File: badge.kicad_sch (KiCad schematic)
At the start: 29 parts, among them J1 SAO V.1.69bis master, Q1 BSS138, SW1 power, SW2 SW_Push, SW3 update epaper, U1 Seeed XIAO ESP32-C3, U2 epaper2.13, U3 5V boost converter, U4 TXS0104EPWR

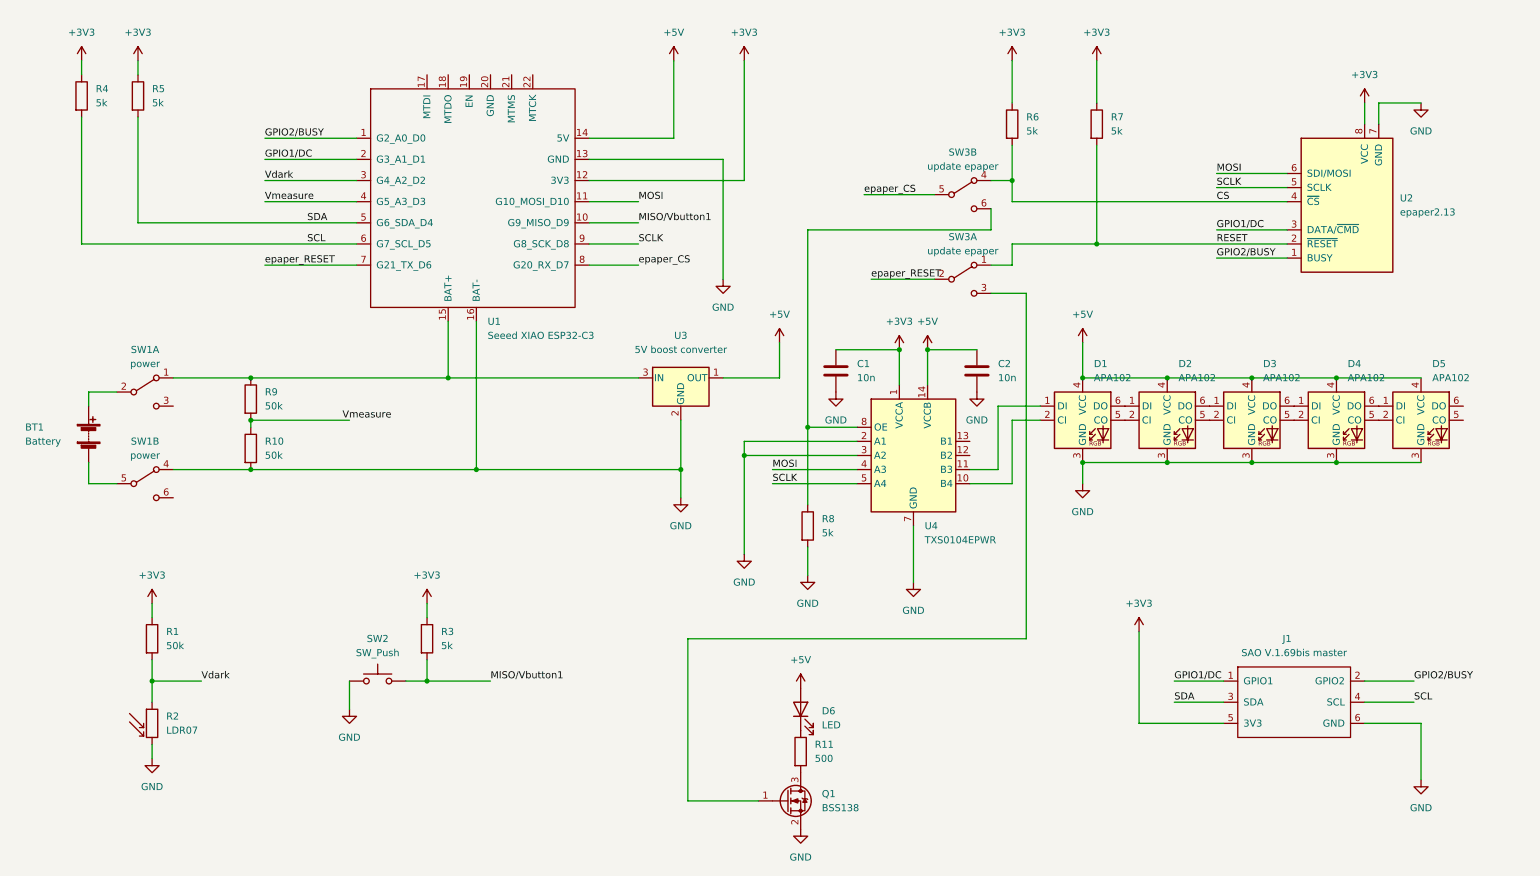
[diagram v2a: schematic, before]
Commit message: disable epaper mod by cutting power (also helps lifetime)
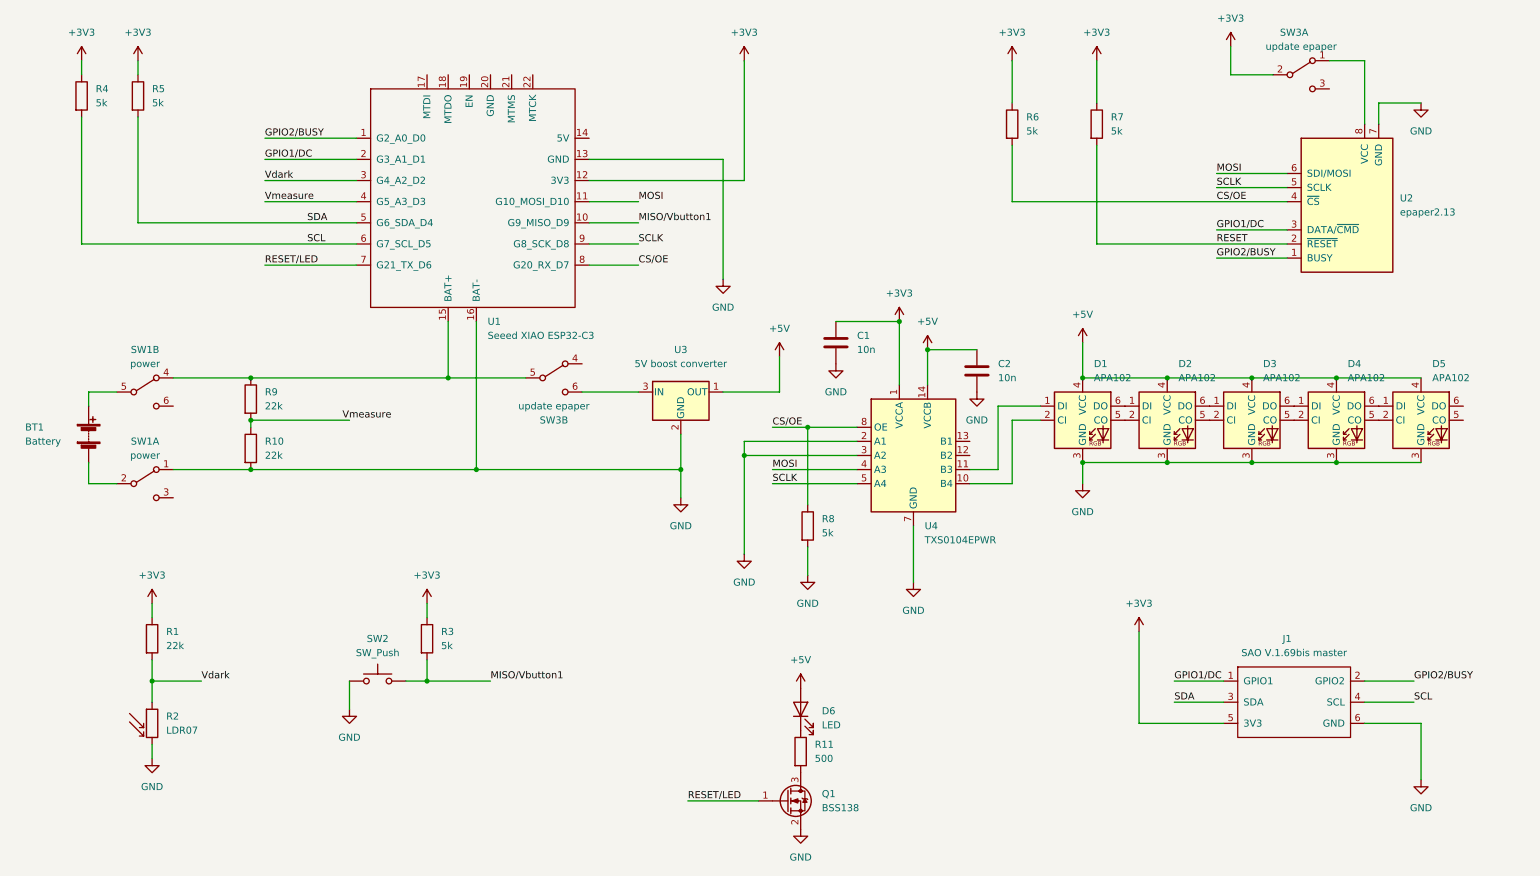
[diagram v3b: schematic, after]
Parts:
- R1, R10, R9: value 50k -> 22k
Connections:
- net +3V3: now also SW3.2 (B); no longer U2.8 (VCC)
- net +5V: no longer U1.14 (5V)
- net GND: now also SW1.1 (A); no longer SW1.4 (A)
- net RESET: no longer SW3.1 (A)
- net at R9.1, U1.15 (BAT+): now also SW1.4 (A), SW3.5 (B); no longer SW1.1 (A), U3.3 (IN)
- net at SW1.2 (B): now also BT1.2 (-); no longer BT1.1 (+)
- net CS/OE: now reaches R8.1, U4.8 (OE)
- net CS/OE: now also R6.2, U1.8 (G20_RX_D7), U2.4 (~{CS}); no longer SW3.6 (C)
- net at SW1.5 (B): now also BT1.1 (+); no longer BT1.2 (-)
- net at SW3.3 (C): no longer Q1.1 (G)
- removed net CS: R6.2, SW3.4 (A), U2.4 (~{CS})
- removed net epaper_CS: SW3.5 (B), U1.8 (G20_RX_D7)
- net epaper_RESET renamed RESET/LED
- net RESET/LED: now also Q1.1 (G); no longer SW3.2 (B)
- new net: SW3.1 (A), U2.8 (VCC)
- new net: SW3.6 (C), U3.3 (IN)
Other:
- moved on the sheet: C1, SW1A, SW1B, SW3A, SW3B, U3

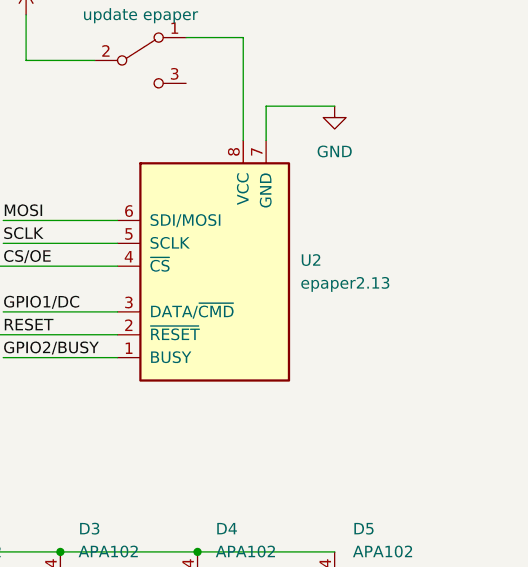
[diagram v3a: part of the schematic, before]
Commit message: use updated epaper footprint
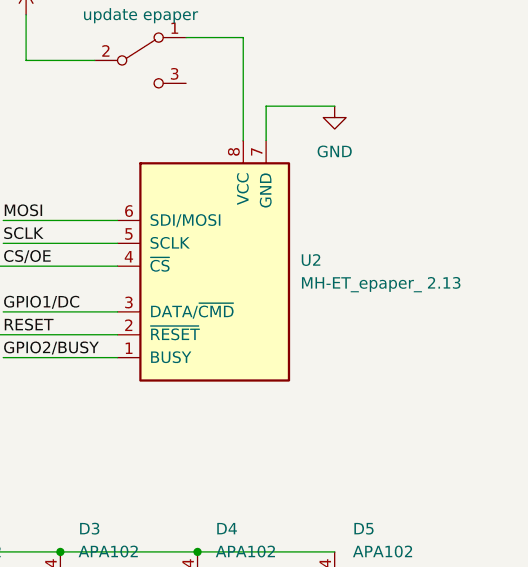
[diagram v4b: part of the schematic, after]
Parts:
- U2: value epaper2.13 -> MH-ET_epaper_ 2.13; footprint extra:epaper2.13 -> extra:MH-ET_epaper_ 2.13; symbol mlp:epaper2.13 -> extra:MH-ET_epaper_ 2.13
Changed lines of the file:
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@@
     (pin "6")
   )
-  (symbol (lib_id "mlp:epaper2.13") (at 254 52.07 0) (unit 1)
+  (symbol (lib_id "extra:MH-ET_epaper_ 2.13") (at 254 52.07 0) (unit 1)
     (in_bom yes) (on_board yes) (fields_autoplaced)
     (property "Reference" "U2" (id 0) (at 264.16 48.8949 0)
       (effects (font (size 1.27 1.27)) (justify left))
     )
-    (property "Value" "epaper2.13" (id 1) (at 264.16 51.4349 0)
-      (effects (font (size 1.27 1.27)) (justify left))
-    )
-    (property "Footprint" "extra:epaper2.13" (id 2) (at 254 66.04 0)
+    (property "Value" "MH-ET_epaper_ 2.13" (id 1) (at 264.16 51.4349 0)
+      (effects (font (size 1.27 1.27)) (justify left))
+    )
+    (property "Footprint" "extra:MH-ET_epaper_ 2.13" (id 2) (at 254 66.04 0)
       (effects (font (size 1.27 1.27)) hide)
     )
@@
     )
     (path "/20ddfe2b-2a25-4b87-9377-bd1690073b28"
-      (reference "U2") (unit 1) (value "epaper2.13") (footprint "extra:epaper2.13")
+      (reference "U2") (unit 1) (value "MH-ET_epaper_ 2.13") (footprint "extra:MH-ET_epaper_ 2.13")
     )
     (path "/45af8bb5-3b53-4556-9240-4d30d2024c6a"

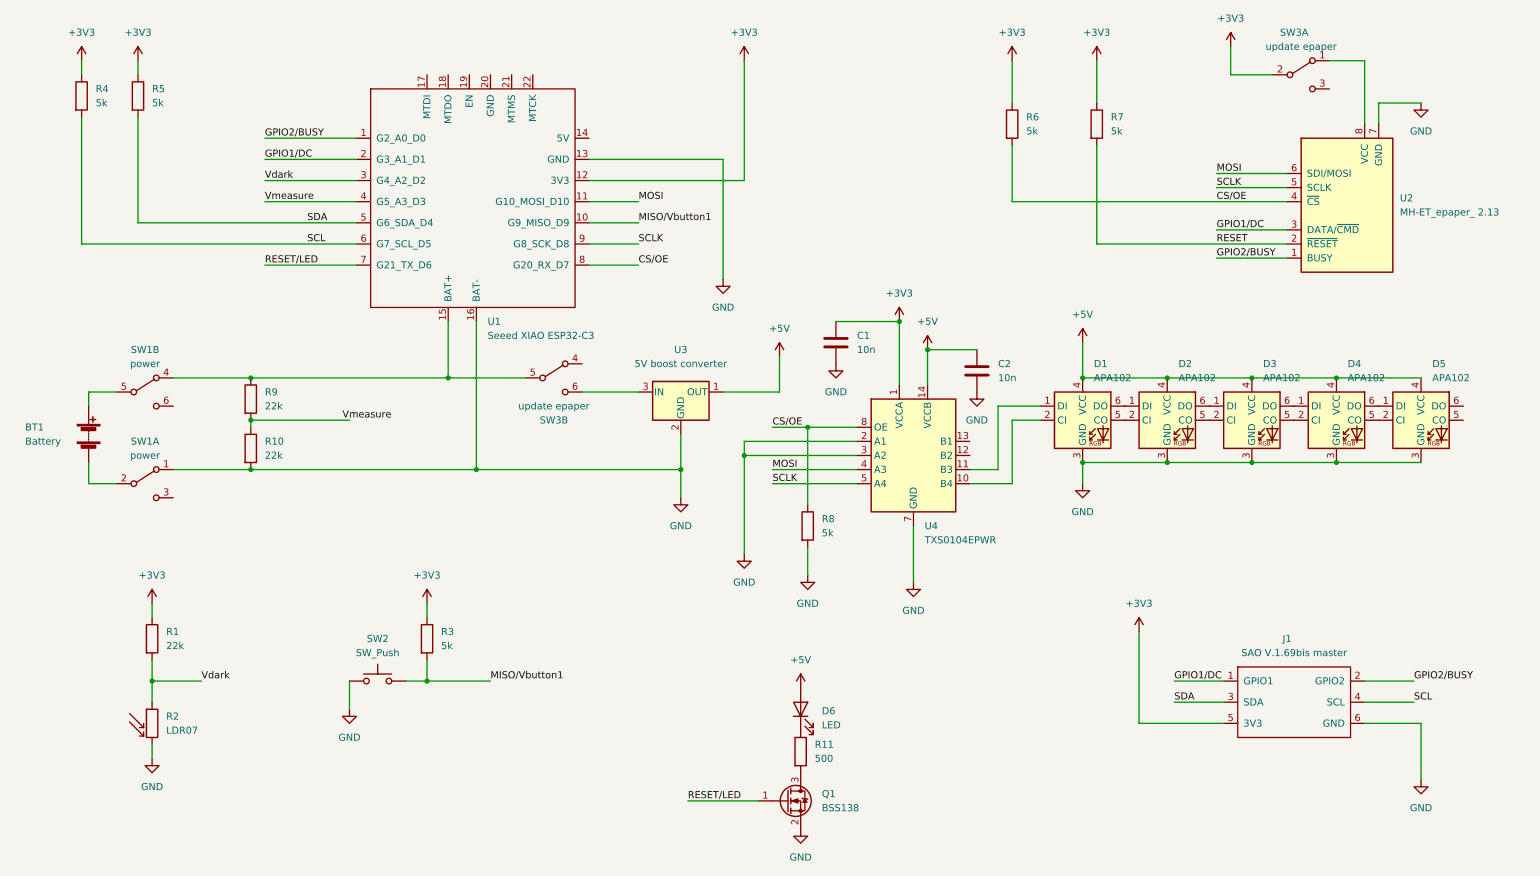
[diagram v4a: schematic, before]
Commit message: improve switch function, label switches
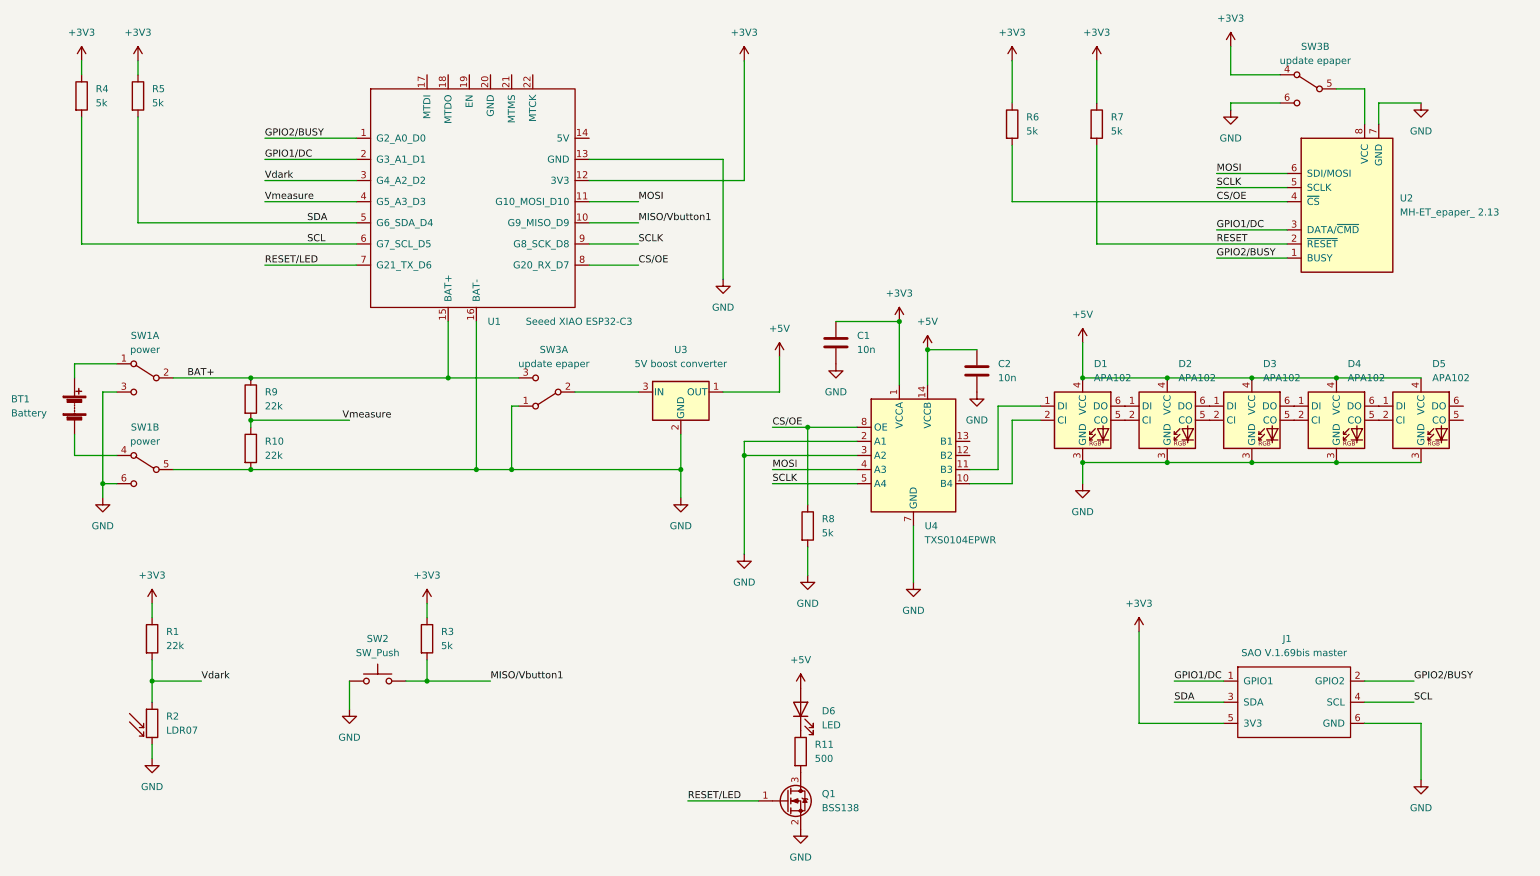
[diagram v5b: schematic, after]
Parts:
- U1: symbol mlp:Seeed XIAO ESP32-C3 -> extra:Seeed XIAO ESP32-C3
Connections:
- net +3V3: now also SW3.4 (A); no longer SW3.2 (B)
- net GND: now also SW1.3 (C), SW1.5 (B), SW1.6 (C), SW3.1 (A), SW3.6 (C); no longer SW1.1 (A)
- net at BT1.2 (-): now also SW1.4 (A); no longer SW1.2 (B)
- net at U2.8 (VCC): now also SW3.5 (B); no longer SW3.1 (A)
- net BAT+: now reaches R9.1, U1.15 (BAT+)
- net BAT+: now also SW1.2 (B), SW3.3 (C); no longer SW1.4 (A), SW3.5 (B)
- net at U3.3 (IN): now also SW3.2 (B); no longer SW3.6 (C)
- net at BT1.1 (+): now also SW1.1 (A); no longer SW1.5 (B)
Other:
- moved on the sheet: BT1, SW1A, SW1B, SW3A, SW3B

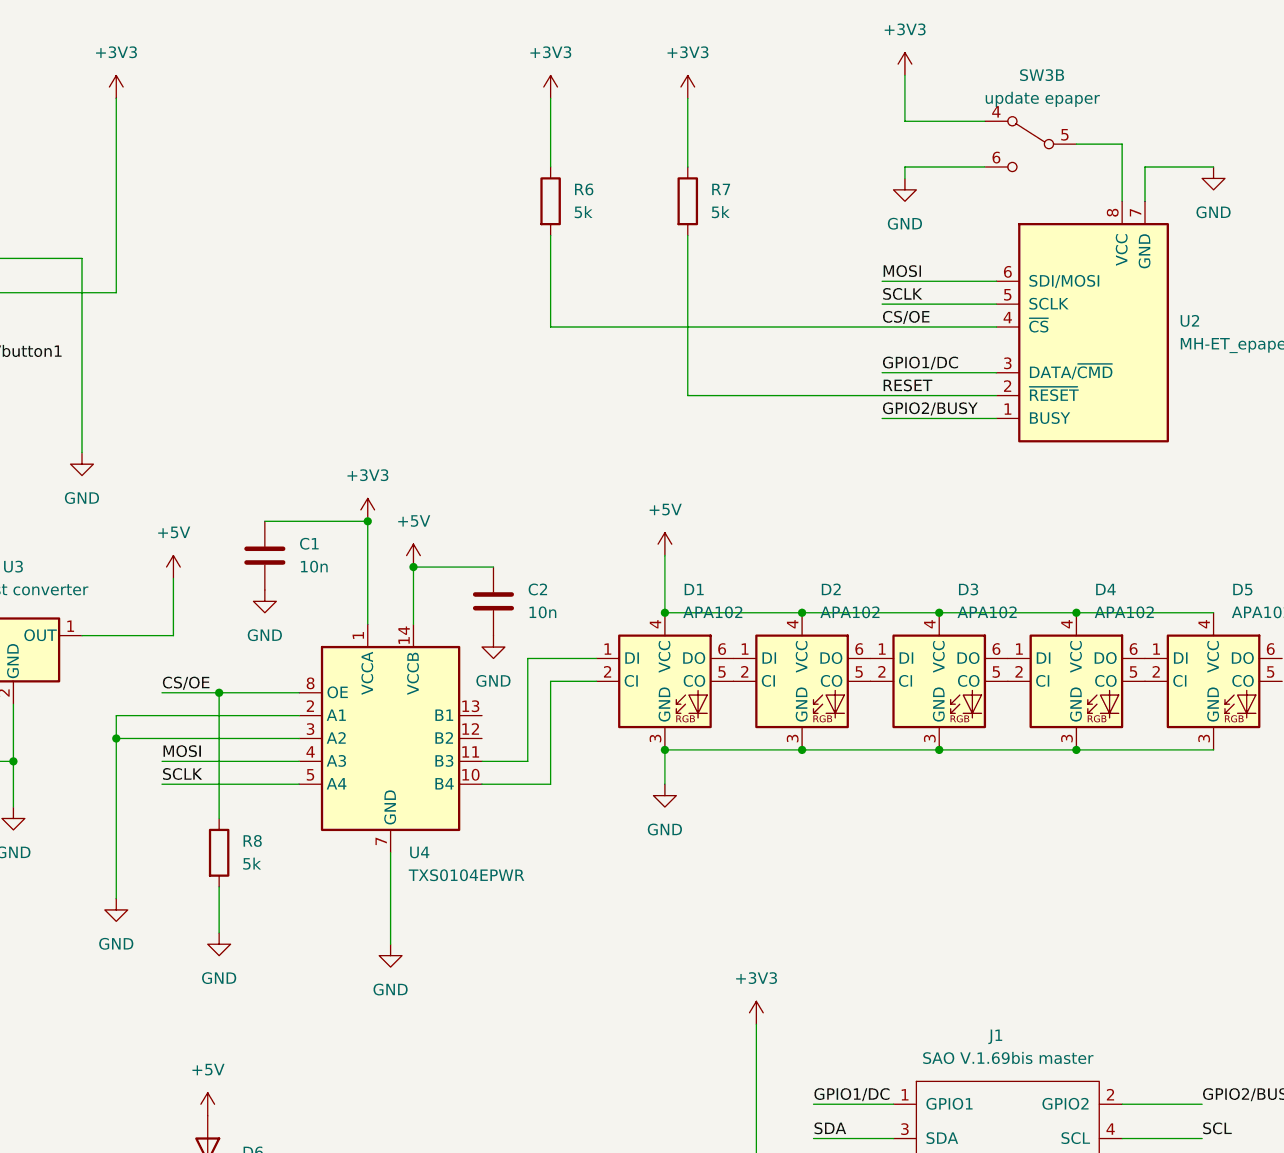
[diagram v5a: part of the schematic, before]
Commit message: fixed fighting pull-up/down on CS/OE but kept paste stencil
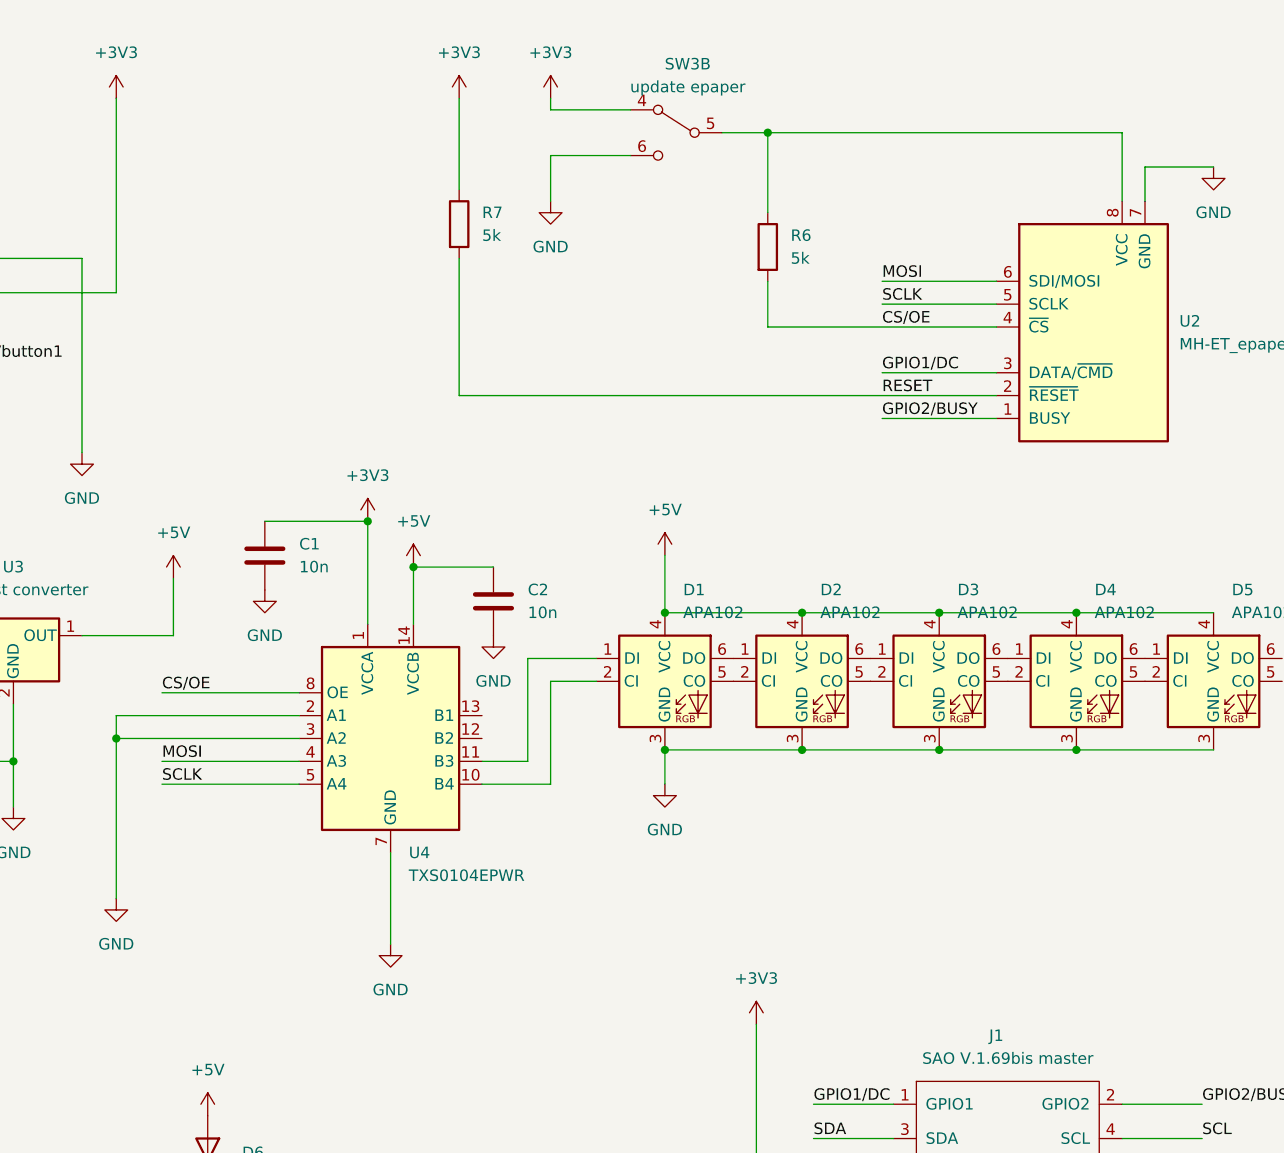
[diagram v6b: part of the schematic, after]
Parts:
- removed R8: 5k, Resistor_SMD:R_2010_5025Metric_Pad1.40x2.65mm_HandSolder, symbol Device:R
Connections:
- net +3V3: no longer R6.1
- net at SW3.5 (B), U2.8 (VCC): now also R6.1
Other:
- moved on the sheet: R6, R7, SW3B
